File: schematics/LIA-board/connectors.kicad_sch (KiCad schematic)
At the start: 3 parts, among them J2 USB_C_Receptacle_PowerOnly_6P, P1 USB_C_Plug_USB2.0

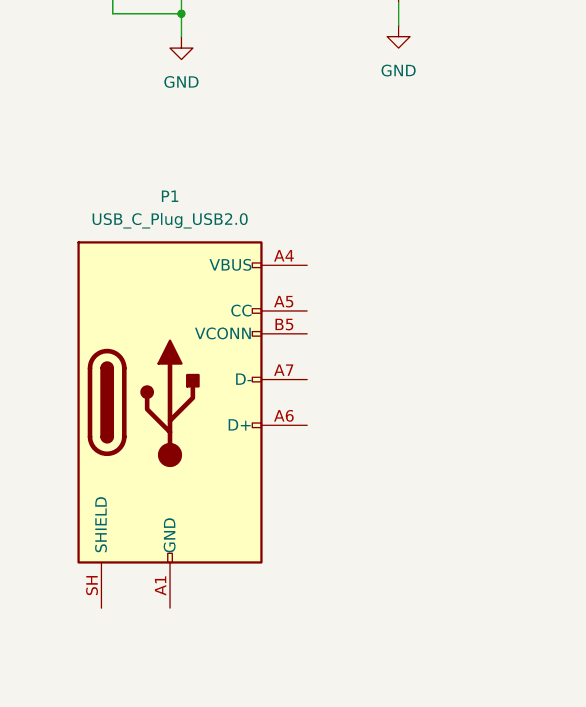
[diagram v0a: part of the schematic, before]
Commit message: new oscillator, not tested in simulation yet
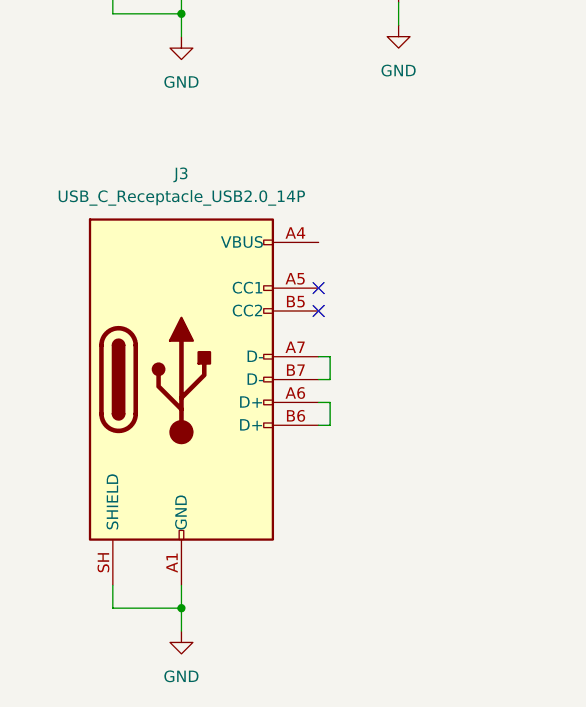
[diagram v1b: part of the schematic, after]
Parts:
- removed P1: USB_C_Plug_USB2.0, symbol Connector:USB_C_Plug_USB2.0
- added J3: USB_C_Receptacle_USB2.0_14P, symbol Connector:USB_C_Receptacle_USB2.0_14P
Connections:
- net GND: now also J3.A1 (GND), J3.A12 (GND), J3.B1 (GND), J3.B12 (GND), J3.SH (SHIELD)
- new net: J3.A4 (VBUS), J3.A9 (VBUS), J3.B4 (VBUS), J3.B9 (VBUS)
- new net: J3.A6 (D+), J3.B6 (D+)
- new net: J3.A7 (D-), J3.B7 (D-)
- no-connect marks 0 -> 2
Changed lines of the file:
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@@
 	(paper "A4")
+	(junction
+		(at 72.39 170.18)
+		(diameter 0)
+		(color 0 0 0 0)
+	)
 	(junction
 		(at 72.39 104.14)
@@
 		(color 0 0 0 0)
 	)
+	(no_connect
+		(at 87.63 134.62)
+	)
+	(no_connect
+		(at 87.63 137.16)
+	)
 	(wire
 		(pts
@@
 	(wire
 		(pts
+			(xy 72.39 170.18) (xy 72.39 167.64)
+		)
+		(stroke
+			(width 0)
+			(type default)
+		)
+	)
+	(wire
+		(pts
 			(xy 99.06 88.9) (xy 107.95 88.9)
 		)
@@
 	(wire
 		(pts
+			(xy 88.9 142.24) (xy 88.9 144.78)
+		)
+		(stroke
+			(width 0)
+			(type default)
+		)
+	)
+	(wire
+		(pts
 			(xy 87.63 88.9) (xy 99.06 88.9)
 		)
@@
 	(wire
 		(pts
+			(xy 72.39 170.18) (xy 72.39 172.72)
+		)
+		(stroke
+			(width 0)
+			(type default)
+		)
+	)
+	(wire
+		(pts
 			(xy 72.39 104.14) (xy 72.39 106.68)
 		)
@@
 	(wire
 		(pts
+			(xy 88.9 147.32) (xy 88.9 149.86)
+		)
+		(stroke
+			(width 0)
+			(type default)
+		)
+	)
+	(wire
+		(pts
+			(xy 87.63 142.24) (xy 88.9 142.24)
+		)
+		(stroke
+			(width 0)
+			(type default)
+		)
+	)
+	(wire
+		(pts
+			(xy 87.63 147.32) (xy 88.9 147.32)
+		)
+		(stroke
+			(width 0)
+			(type default)
+		)
+	)
+	(wire
+		(pts
+			(xy 64.77 167.64) (xy 64.77 170.18)
+		)
+		(stroke
+			(width 0)
+			(type default)
+		)
+	)
+	(wire
+		(pts
 			(xy 64.77 101.6) (xy 64.77 104.14)
 		)
@@
 	(wire
 		(pts
+			(xy 87.63 144.78) (xy 88.9 144.78)
+		)
+		(stroke
+			(width 0)
+			(type default)
+		)
+	)
+	(wire
+		(pts
 			(xy 99.06 88.9) (xy 99.06 92.71)
 		)
@@
 		(pts
 			(xy 87.63 91.44) (xy 93.98 91.44)
+		)
+		(stroke
+			(width 0)
+			(type default)
+		)
+	)
+	(wire
+		(pts
+			(xy 88.9 149.86) (xy 87.63 149.86)
+		)
+		(stroke
+			(width 0)
+			(type default)
+		)
+	)
+	(wire
+		(pts
+			(xy 64.77 170.18) (xy 72.39 170.18)
 		)
 		(stroke
@@
 	)
 	(symbol
-		(lib_id "Connector:USB_C_Plug_USB2.0")
-		(at 71.12 147.32 0)
+		(lib_id "power:GND")
+		(at 72.39 172.72 0)
 		(unit 1)
 		(body_style 1)
@@
 		(dnp no)
 		(fields_autoplaced yes)
-		(property "Reference" "P1"
-			(at 71.12 124.46 0)
-			(show_name no)
-			(do_not_autoplace no)
-			(effects
-				(font
-					(size 1.27 1.27)
-				)
-			)
-		)
-		(property "Value" "USB_C_Plug_USB2.0"
-			(at 71.12 127 0)
+		(property "Reference" "#PWR0126"
+			(at 72.39 179.07 0)
+			(hide yes)
+			(show_name no)
+			(do_not_autoplace no)
+			(effects
+				(font
+					(size 1.27 1.27)
+				)
+			)
+		)
+		(property "Value" "GND"
+			(at 72.39 177.8 0)
 			(show_name no)
 			(do_not_autoplace no)
@@
 		)
 		(property "Footprint" ""
-			(at 74.93 147.32 0)
-			(hide yes)
-			(show_name no)
-			(do_not_autoplace no)
-			(effects
-				(font
-					(size 1.27 1.27)
-				)
-			)
-		)
-		(property "Datasheet" "https://www.usb.org/sites/default/files/documents/usb_type-c.zip"
-			(at 74.93 147.32 0)
-			(hide yes)
-			(show_name no)
-			(do_not_autoplace no)
-			(effects
-				(font
-					(size 1.27 1.27)
-				)
-			)
-		)
-		(property "Description" "USB 2.0-only Type-C Plug connector"
-			(at 71.12 147.32 0)
-			(hide yes)
-			(show_name no)
-			(do_not_autoplace no)
-			(effects
-				(font
-					(size 1.27 1.27)
-				)
-			)
-		)
-		(pin "B12"
-		)
-		(pin "SH"
-		)
-		(pin "A9"
-		)
-		(pin "A1"
-		)
-		(pin "A5"
-		)
-		(pin "B5"
-		)
-		(pin "A4"
-		)
-		(pin "B4"
-		)
-		(pin "A12"
-		)
-		(pin "A6"
-		)
-		(pin "B9"
-		)
-		(pin "B1"
-		)
-		(pin "A7"
+			(at 72.39 172.72 0)
+			(hide yes)
+			(show_name no)
+			(do_not_autoplace no)
+			(effects
+				(font
+					(size 1.27 1.27)
+				)
+			)
+		)
+		(property "Datasheet" ""
+			(at 72.39 172.72 0)
+			(hide yes)
+			(show_name no)
+			(do_not_autoplace no)
+			(effects
+				(font
+					(size 1.27 1.27)
+				)
+			)
+		)
+		(property "Description" "Power symbol creates a global label with name \"GND\" , ground"
+			(at 72.39 172.72 0)
+			(hide yes)
+			(show_name no)
+			(do_not_autoplace no)
+			(effects
+				(font
+					(size 1.27 1.27)
+				)
+			)
+		)
+		(pin "1"
 		)
 		(instances
 			(project "GMOS-LIA"
 				(path "/87b3d1ed-39bd-4cff-a405-e580c48ff0ef/bc9db269-b6e3-4963-a650-1fdcbd7049f2"
-					(reference "P1")
+					(reference "#PWR0126")
 					(unit 1)
 				)
@@
 					(unit 1)
 				)
+			)
+		)
+	)
+	(symbol
+		(lib_id "Connector:USB_C_Receptacle_USB2.0_14P")
+		(at 72.39 144.78 0)
+		(unit 1)
+		(body_style 1)
+		(exclude_from_sim no)
+		(in_bom yes)
+		(on_board yes)
+		(in_pos_files yes)
+		(dnp no)
+		(fields_autoplaced yes)
+		(property "Reference" "J3"
+			(at 72.39 121.92 0)
+			(show_name no)
+			(do_not_autoplace no)
+			(effects
+				(font
+					(size 1.27 1.27)
+				)
+			)
+		)
+		(property "Value" "USB_C_Receptacle_USB2.0_14P"
+			(at 72.39 124.46 0)
+			(show_name no)
+			(do_not_autoplace no)
+			(effects
+				(font
+					(size 1.27 1.27)
+				)
+			)
+		)
+		(property "Footprint" ""
+			(at 76.2 144.78 0)
+			(hide yes)
+			(show_name no)
+			(do_not_autoplace no)
+			(effects
+				(font
+					(size 1.27 1.27)
+				)
+			)
+		)
+		(property "Datasheet" "https://www.usb.org/sites/default/files/documents/usb_type-c.zip"
+			(at 76.2 144.78 0)
+			(hide yes)
+			(show_name no)
+			(do_not_autoplace no)
+			(effects
+				(font
+					(size 1.27 1.27)
+				)
+			)
+		)
+		(property "Description" "USB 2.0-only 14P Type-C Receptacle connector"
+			(at 72.39 144.78 0)
+			(hide yes)
+			(show_name no)
+			(do_not_autoplace no)
+			(effects
+				(font
+					(size 1.27 1.27)
+				)
+			)
+		)
+		(pin "B5"
+		)
+		(pin "A9"
+		)
+		(pin "B6"
+		)
+		(pin "A7"
+		)
+		(pin "B9"
+		)
+		(pin "A6"
+		)
+		(pin "B1"
+		)
+		(pin "B4"
+		)
+		(pin "A5"
+		)
+		(pin "SH"
+		)
+		(pin "A1"
+		)
+		(pin "B12"
+		)
+		(pin "A4"
+		)
+		(pin "B7"
+		)
+		(pin "A12"
+		)
+		(instances
+			(project "GMOS-LIA"
+				(path "/87b3d1ed-39bd-4cff-a405-e580c48ff0ef/bc9db269-b6e3-4963-a650-1fdcbd7049f2"
+					(reference "J3")
+					(unit 1)
+				)

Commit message: commit before changing LIA
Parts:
- removed J3: USB_C_Receptacle_USB2.0_14P, symbol Connector:USB_C_Receptacle_USB2.0_14P
- added D8: SMAJ18A, Diode_SMD:D_SMA, symbol Diode:SMAJ18A
- added J4: ${FAMILY}, symbol CERN:Terminal Block_2 Positions_Screw Connection
- added J5, J6: Conn_01x05_Pin, symbol Connector:Conn_01x05_Pin
- renumbered D1 to D3, J2 to J1
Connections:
- net GND: now also D8.2 (A2), J4.1, J5.5 (Pin_5)
- net VBUS renamed VBUS_PD
- net VBUS_PD: now also D8.1 (A1)
- new net +3V3_D: J5.1 (Pin_1)
- new net Vcc_FTDI: J6.1 (Pin_1)
- new net Vin: J4.2
- new net iso_gnd: J6.4 (Pin_4)
- new net mcu_rst: J5.4 (Pin_4)
- new net swclk_in: J5.3 (Pin_3)
- new net swdio_in: J5.2 (Pin_2)
- new net uart_rx_iso: J6.3 (Pin_3)
- new net uart_tx_iso: J6.2 (Pin_2)
- no-connect marks 2 -> 1
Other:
- moved on the sheet: D3, J1
